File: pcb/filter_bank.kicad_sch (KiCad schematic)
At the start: 64 parts, among them K1 G6K-2F-Y-DC5, K2 G6K-2F-Y-DC5, K3 G6K-2F-Y-DC5, K4 G6K-2F-Y-DC5, K5 G6K-2F-Y-DC5, K6 G6K-2F-Y-DC5, K7 G6K-2F-Y-DC5, K8 G6K-2F-Y-DC5, Q6 2N7002, Q7 2N7002, Q8 2N7002, Q9 2N7002

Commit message: Replace Empyrean SAMD21 module with AVR128DA32 + CP2102N USB-C/UPDI (from Si5351AVFO)
- New sheet mcu_usb: AVR128DA32-I/PT, 32.768k crystal on PF0/PF1 with 15p loads,
  USB-C + SP0503 ESD, CP2102N with DTR auto-reset, LP2985-3.3, UPDI header
- Remove U7 Empyrean from root sheet
- Relay drivers Q6-Q9: 2N7002 -> AO3400A for 3.3 V gate drive
- ERC 0 errors; schematic PDF regenerated; docs/VERIFY.md open items
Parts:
- Q6, Q7, Q8, Q9: value 2N7002 -> AO3400A; LCSC C8545 -> C20917; MPN 2N7002 -> AO3400A; Manufacturer (none) -> Alpha & Omega Semicon
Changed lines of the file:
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@@
 			)
 		)
-		(property "Value" "2N7002"
+		(property "Value" "AO3400A"
 			(at 45.72 158.48 0)
 			(effects
@@
 			)
 		)
-		(property "MPN" "2N7002"
+		(property "MPN" "AO3400A"
 			(at 40.64 157.48 0)
 			(effects
@@
 			)
 		)
-		(property "LCSC" "C8545"
+		(property "Manufacturer" "Alpha & Omega Semicon"
+			(at 40.64 157.48 0)
+			(effects
+				(font
+					(size 1.27 1.27)
+				)
+				(hide yes)
+			)
+		)
+		(property "LCSC" "C20917"
 			(at 40.64 157.48 0)
 			(effects
@@
 			)
 		)
-		(property "Value" "2N7002"
+		(property "Value" "AO3400A"
 			(at 83.82 158.48 0)
 			(effects
@@
 			)
 		)
-		(property "MPN" "2N7002"
+		(property "MPN" "AO3400A"
 			(at 78.74 157.48 0)
 			(effects
@@
 			)
 		)
-		(property "LCSC" "C8545"
+		(property "Manufacturer" "Alpha & Omega Semicon"
+			(at 78.74 157.48 0)
+			(effects
+				(font
+					(size 1.27 1.27)
+				)
+				(hide yes)
+			)
+		)
+		(property "LCSC" "C20917"
 			(at 78.74 157.48 0)
 			(effects
@@
 			)
 		)
-		(property "Value" "2N7002"
+		(property "Value" "AO3400A"
 			(at 121.92 158.48 0)
 			(effects
@@
 			)
 		)
-		(property "MPN" "2N7002"
+		(property "MPN" "AO3400A"
 			(at 116.84 157.48 0)
 			(effects
@@
 			)
 		)
-		(property "LCSC" "C8545"
+		(property "Manufacturer" "Alpha & Omega Semicon"
+			(at 116.84 157.48 0)
+			(effects
+				(font
+					(size 1.27 1.27)
+				)
+				(hide yes)
+			)
+		)
+		(property "LCSC" "C20917"
 			(at 116.84 157.48 0)
 			(effects
@@
 			)
 		)
-		(property "Value" "2N7002"
+		(property "Value" "AO3400A"
 			(at 160.02 158.48 0)
 			(effects
@@
 			)
 		)
-		(property "MPN" "2N7002"
+		(property "MPN" "AO3400A"
 			(at 154.94 157.48 0)
 			(effects
@@
 			)
 		)
-		(property "LCSC" "C8545"
+		(property "Manufacturer" "Alpha & Omega Semicon"
 			(at 154.94 157.48 0)
 			(effects
+				(font
+					(size 1.27 1.27)
+				)
+				(hide yes)
+			)
+		)
+		(property "LCSC" "C20917"
+			(at 154.94 157.48 0)
+			(effects

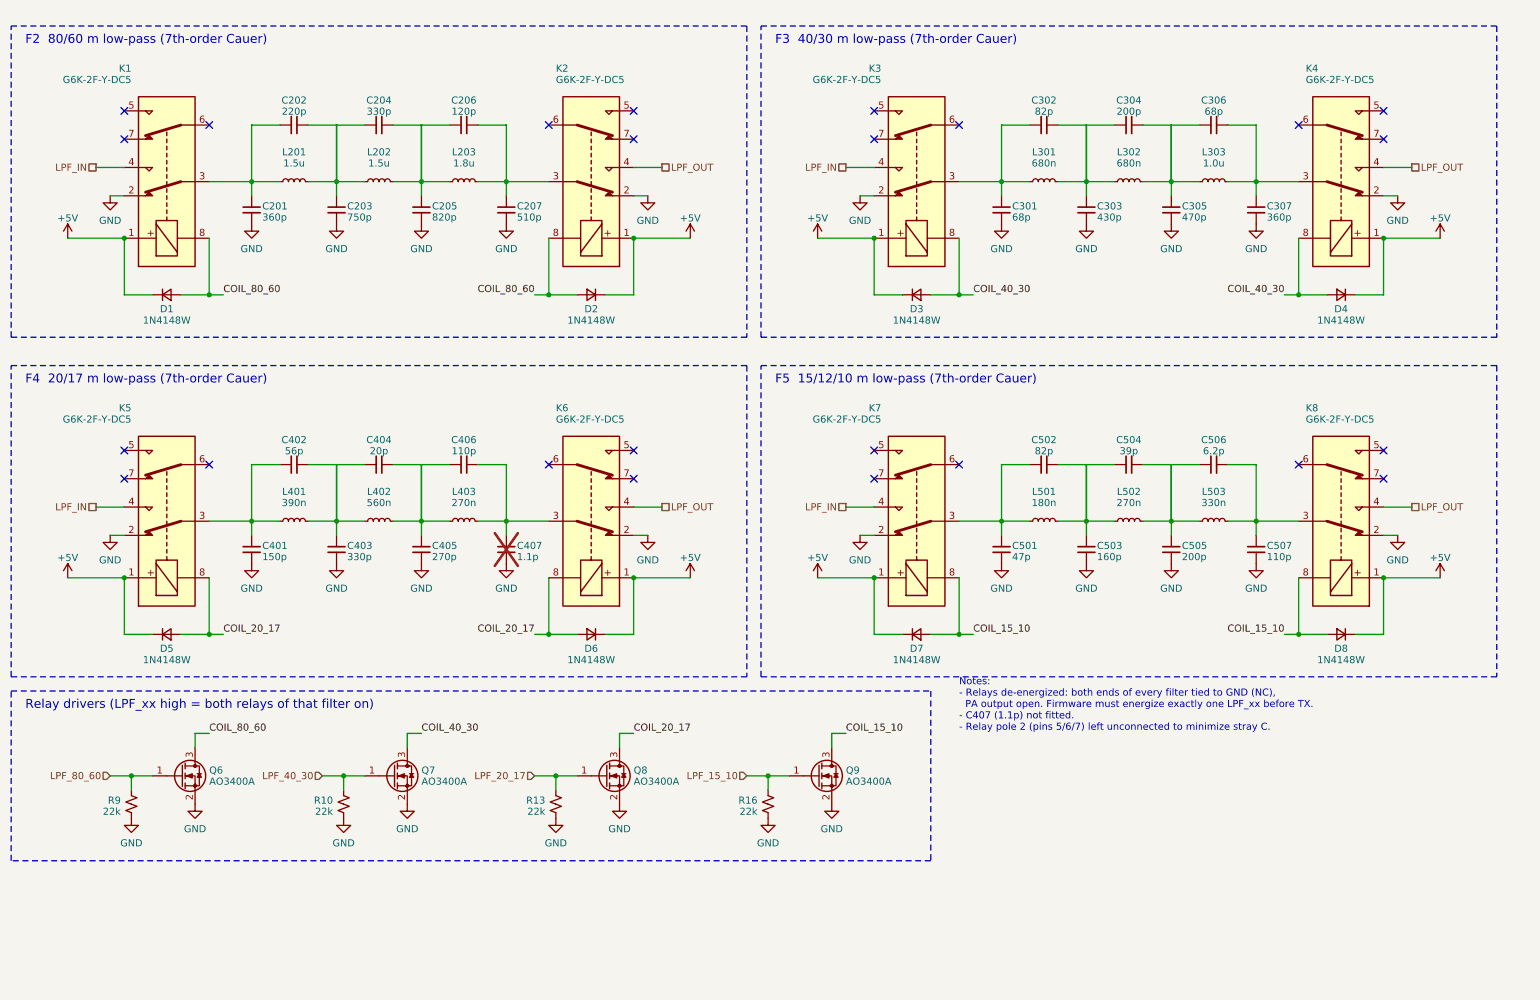
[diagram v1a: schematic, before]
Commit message: Filter bank: 6-relay two-level tree driven by BAND_A/BAND_B
Replace the 8-relay, 4-driver bank with a 2-bit tree (K1-K3 input,
K4-K6 output, one G6K pole each). All relays off selects 80/60 m.
Q6/Q7 AO3400A drive the first and second levels; PA7/PC2 freed.
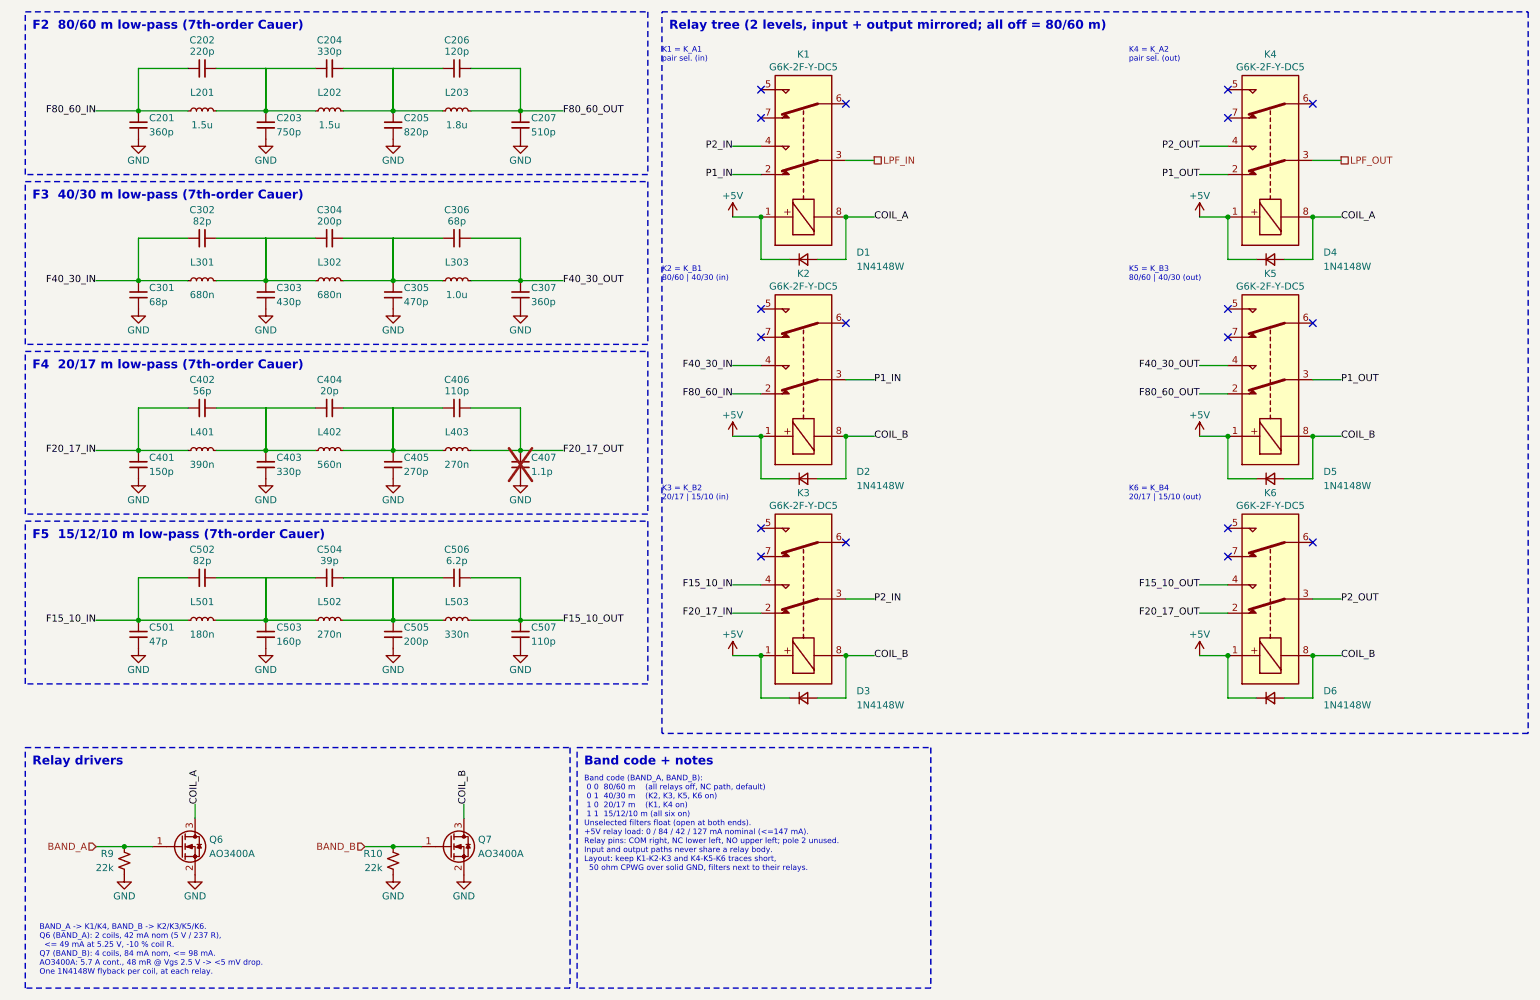
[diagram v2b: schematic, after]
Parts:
- removed D7, D8: 1N4148W, Diode_SMD:D_SOD-123, symbol Device:D_Small
- removed K7, K8: G6K-2F-Y-DC5, Relay_SMD:Relay_DPDT_Omron_G6K-2F-Y, symbol Relay:G6K-2
- removed Q8, Q9: AO3400A, Package_TO_SOT_SMD:SOT-23, symbol Transistor_FET:2N7002
- removed R13, R16: 22k, Resistor_SMD:R_0603_1608Metric, symbol Device:R_Small_US
- C201, C202, C204, C205, C206, C301, C302, C304, C305, C306, C307, C401, C402, C403, C404, C405, C406, C501, C502, C503, C504, C505, C507: Tolerance 2% -> (none)
- C203, C207, C303: Tolerance 1% -> (none)
- C407: Tolerance DNP -> (none)
- C506: Tolerance 0.25pF -> (none)
- K1, K2, K3, K4, K5, K6: Alt HFD4/5-SR (LCSC C64399) -> (none)
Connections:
- net GND: no longer K1.2, K2.2, K3.2, K4.2, K5.2, K6.2
- net LPF_IN: now also K1.3; no longer K1.4, K3.4, K5.4
- net LPF_OUT: now also K4.3; no longer K2.4, K4.4, K6.4
- net F40_30_OUT: now reaches C306.2, C307.1, L303.2
- net F40_30_OUT: now also K5.4; no longer K4.3
- net F80_60_OUT: now reaches C206.2, C207.1, L203.2
- net F80_60_OUT: now also K5.2; no longer K2.3
- net F15_10_IN: now reaches C501.1, C502.1, L501.1
- net F15_10_IN: now also K3.4
- net F40_30_IN: now reaches C301.1, C302.1, L301.1
- net F40_30_IN: now also K2.4; no longer K3.3
- net F15_10_OUT: now reaches C506.2, C507.1, L503.2
- net F15_10_OUT: now also K6.4
- net F20_17_OUT: now reaches C406.2, C407.1, L403.2
- net F20_17_OUT: now also K6.2; no longer K6.3
- net F20_17_IN: now reaches C401.1, C402.1, L401.1
- net F20_17_IN: now also K3.2; no longer K5.3
- net F80_60_IN: now reaches C201.1, C202.1, L201.1
- net F80_60_IN: now also K2.2; no longer K1.3
- net COIL_20_17 renamed COIL_B
- net COIL_B: now also D2.2 (A), D3.2 (A), K2.8, K3.8, Q7.3 (D)
- removed net COIL_40_30: D3.2 (A), D4.2 (A), K3.8, K4.8, Q7.3 (D)
- net COIL_80_60 renamed COIL_A
- net COIL_A: now also D4.2 (A), K4.8; no longer D2.2 (A), K2.8
- net LPF_40_30 renamed BAND_B
- net LPF_80_60 renamed BAND_A
- new net P1_IN: K1.2, K2.3
- new net P1_OUT: K4.2, K5.3
- new net P2_IN: K1.4, K3.3
- new net P2_OUT: K4.4, K6.3
- no-connect marks 24 -> 18
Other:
- note added: "BAND_A -> K1/K4, BAND_B -> K2/K3/K5/K6. Q6 (BAND_A): 2 coils, 42 mA nom (5 V / 237 R), <= 49 mA at 5.25 V, -10 % coil R. Q7 (BAND_B): 4 coils, 84 mA nom, <= 98 mA. AO3400A: 5.7 A cont., 48 mR @ Vgs 2.5 V -> <5 mV drop. One 1N4148W flyback per coil, at each relay."
- note added: "Band code (BAND_A, BAND_B): 0 0 80/60 m (all relays off, NC path, default) 0 1 40/30 m (K2, K3, K5, K6 on) 1 0 20/17 m (K1, K4 on) 1 1 15/12/10 m (all six on) Unselected filters float (open at both ends). +5V relay load: 0 / 84 / 42 / 127 mA nominal (<=147 mA). Relay pins: COM right, NC lower left, NO upper left; pole 2 unused. Input and output paths never share a relay body. Layout: keep K1-K2-K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"
- note added: "Band code + notes"
- note added: "K1 = K_A1 pair sel. (in)"
- note added: "K2 = K_B1 80/60 | 40/30 (in)"
- note added: "K3 = K_B2 20/17 | 15/10 (in)"
- note added: "K4 = K_A2 pair sel. (out)"
- note added: "K5 = K_B3 80/60 | 40/30 (out)"
- note added: "K6 = K_B4 20/17 | 15/10 (out)"
- note added: "Relay drivers"
- note added: "Relay tree (2 levels, input + output mirrored; all off = 80/60 m)"
- note removed: "Notes: - Relays de-energized: both ends of every filter tied to GND (NC), PA output open. Firmware must energize exactly one LPF_xx before TX. - C407 (1.1p) not fitted. - Relay pole 2 (pins 5/6/7) left unconnected to minimize stray C."
- note removed: "Relay drivers (LPF_xx high = both relays of that filter on)"
